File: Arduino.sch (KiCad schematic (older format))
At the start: 23 parts

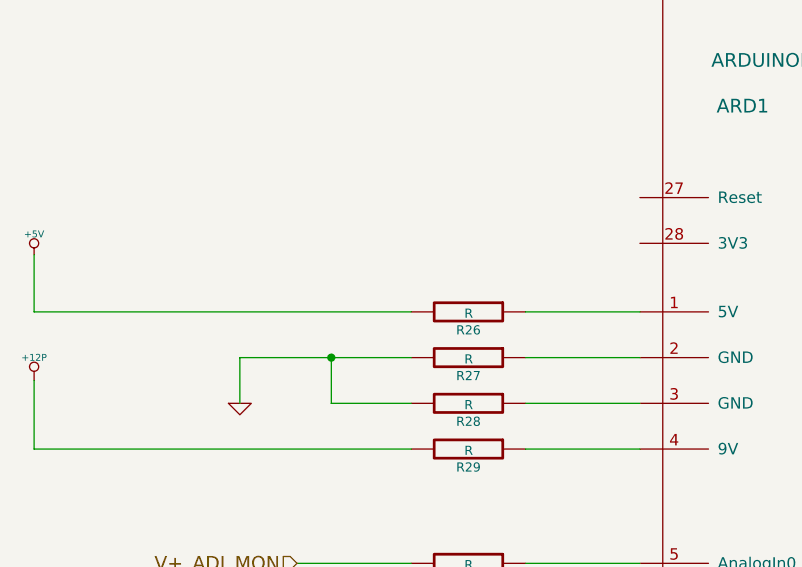
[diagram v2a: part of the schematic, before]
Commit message: Layout Work Session 16
Added ground connect to heatsink, fixed relay trace width, fixed silk
screen issues.
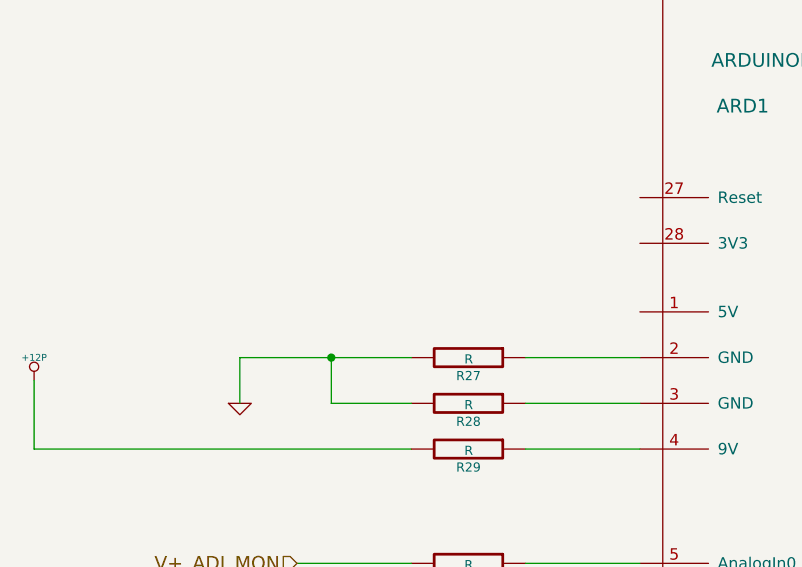
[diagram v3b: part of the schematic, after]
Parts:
- removed R26: R, ~, symbol R
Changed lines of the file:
@@
-EESchema Schematic File Version 2  date 11/24/2013 8:21:44 PM
+EESchema Schematic File Version 2  date 12/1/2013 9:10:28 PM
 LIBS:power
 LIBS:device
@@
 Sheet 8 9
 Title ""
-Date "24 nov 2013"
+Date "2 dec 2013"
 Rev ""
 Comp ""
@@
 	8500 5700 8500 6100
 $Comp
-L GND #PWR041
+L GND #PWR52
 U 1 1 524020EC
 P 8500 6100
-F 0 "#PWR041" H 8500 6100 30  0001 C CNN
+F 0 "#PWR52" H 8500 6100 30  0001 C CNN
 F 1 "GND" H 8500 6030 30  0001 C CNN
 F 2 "~" H 8500 6100 60  0000 C CNN
@@
 	3350 4350 3850 4350
 $Comp
-L +12P #PWR042
+L +12P #PWR50
 U 1 1 5243CFCD
 P 1200 4050
-F 0 "#PWR042" H 1200 4020 30  0001 C CNN
+F 0 "#PWR50" H 1200 4020 30  0001 C CNN
 F 1 "+12P" H 1200 4150 30  0000 C CNN
 F 2 "~" H 1200 4050 60  0000 C CNN
@@
 Wire Wire Line
 	1200 4350 2850 4350
-$Comp
-L R R26
-U 1 1 5245171E
-P 3100 3750
-F 0 "R26" V 3180 3750 40  0000 C CNN
-F 1 "R" V 3107 3751 40  0000 C CNN
-F 2 "~" V 3030 3750 30  0000 C CNN
-F 3 "~" H 3100 3750 30  0000 C CNN
-	1    3100 3750
-	0    1    1    0
-$EndComp
-Wire Wire Line
-	3350 3750 3850 3750
-$Comp
-L +5V #PWR043
-U 1 1 5245176C
-P 1200 3500
-F 0 "#PWR043" H 1200 3590 20  0001 C CNN
-F 1 "+5V" H 1200 3590 30  0000 C CNN
-F 2 "~" H 1200 3500 60  0000 C CNN
-F 3 "~" H 1200 3500 60  0000 C CNN
-	1    1200 3500
-	1    0    0    -1
-$EndComp
-Wire Wire Line
-	2850 3750 1200 3750
-Wire Wire Line
-	1200 3750 1200 3500
 Wire Wire Line
 	3850 3950 3350 3950
@@
 	2100 3950 2100 4150
 $Comp
-L GND #PWR044
+L GND #PWR51
 U 1 1 5245181B
 P 2100 4150
-F 0 "#PWR044" H 2100 4150 30  0001 C CNN
+F 0 "#PWR51" H 2100 4150 30  0001 C CNN
 F 1 "GND" H 2100 4080 30  0001 C CNN
 F 2 "~" H 2100 4150 60  0000 C CNN

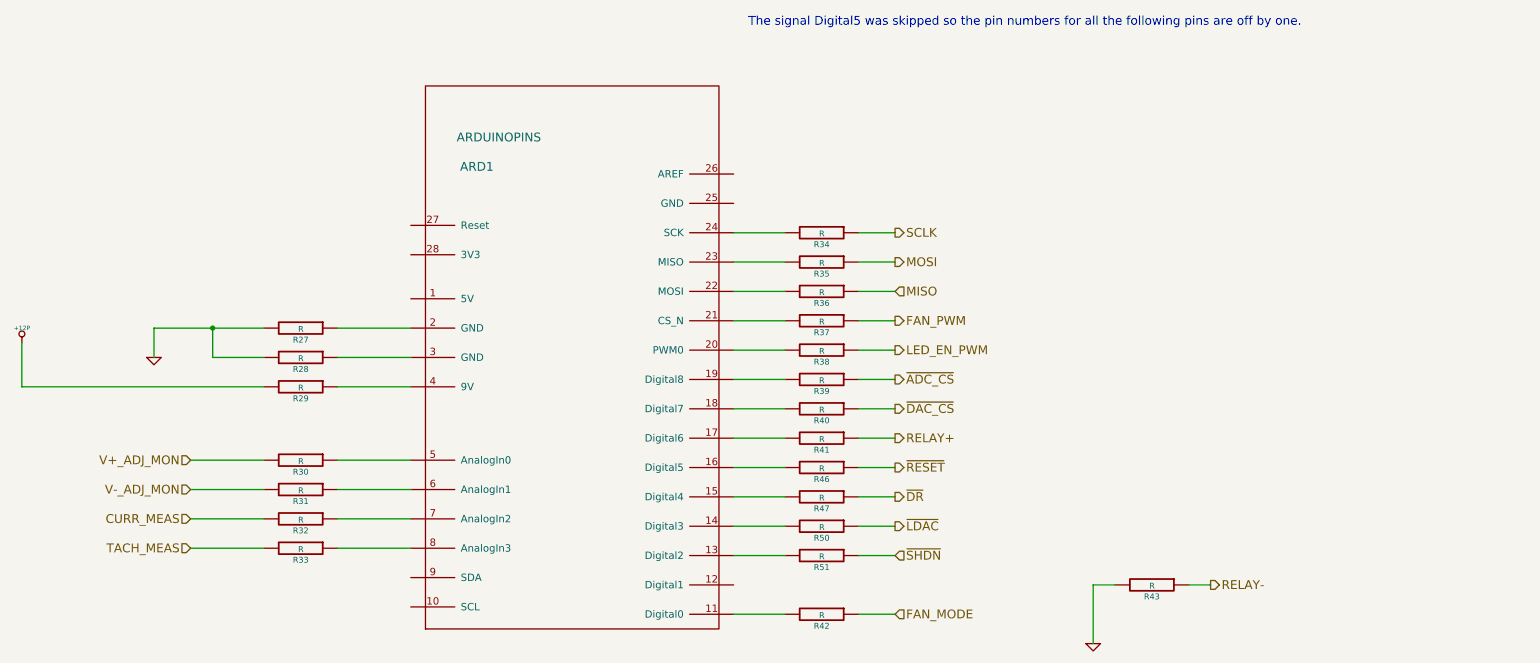
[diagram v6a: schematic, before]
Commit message: Added Passive Values and SPICE models
As part of week 1 of Session 1B, we added a SPICE model of the In amp
and went through and assigned values to all of the passive components.
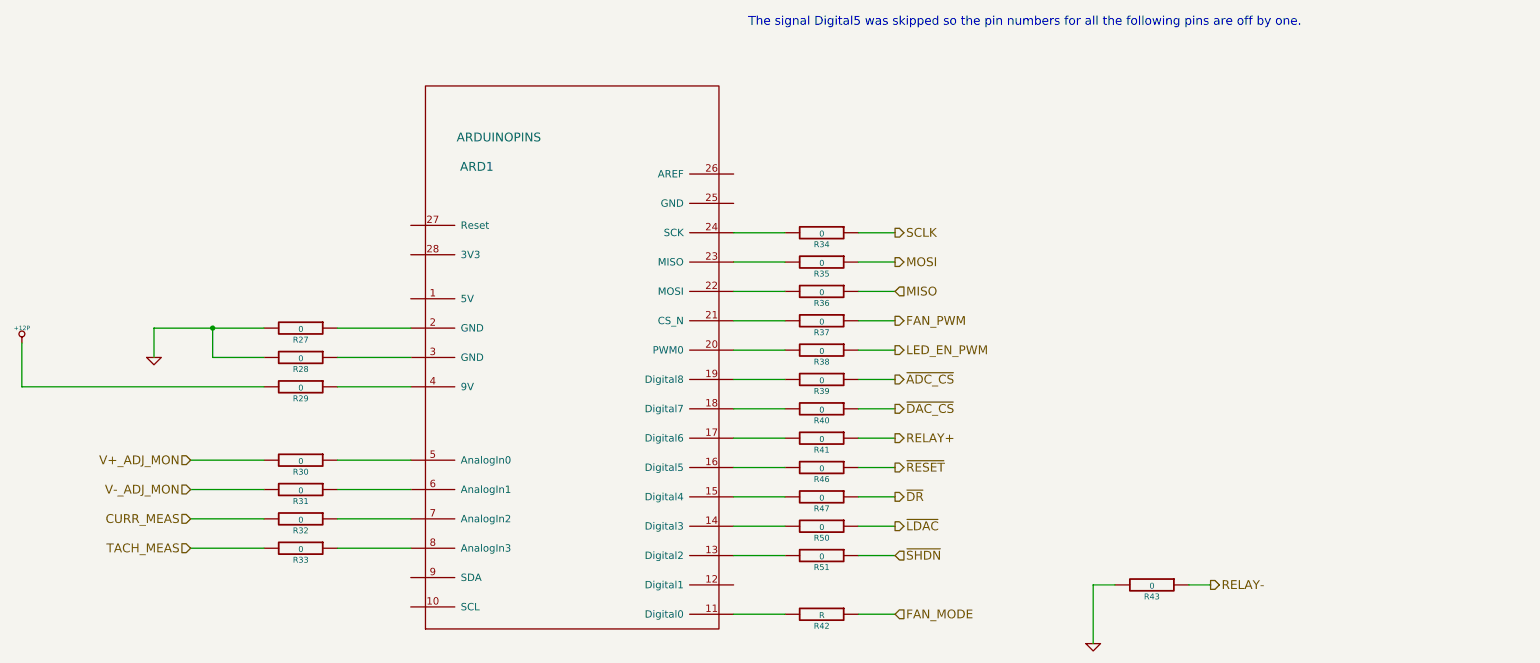
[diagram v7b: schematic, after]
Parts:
- R27, R28, R29, R30, R31, R32, R33, R34, R35, R36, R37, R38, R39, R40, R41, R43, R46, R47, R50, R51: value R -> 0
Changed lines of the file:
@@
-EESchema Schematic File Version 2  date 2/16/2014 3:41:32 PM
+EESchema Schematic File Version 2  date 4/16/2014 11:04:06 PM
 LIBS:power
 LIBS:device
@@
 Sheet 8 9
 Title ""
-Date "16 feb 2014"
+Date "17 apr 2014"
 Rev ""
 Comp ""
@@
 P 6650 3900
 F 0 "R37" V 6730 3900 40  0000 C CNN
-F 1 "R" V 6657 3901 40  0000 C CNN
+F 1 "0" V 6657 3901 40  0000 C CNN
 F 2 "~" V 6580 3900 30  0000 C CNN
 F 3 "~" H 6650 3900 30  0000 C CNN
@@
 P 6650 4700
 F 0 "R41" V 6730 4700 40  0000 C CNN
-F 1 "R" V 6657 4701 40  0000 C CNN
+F 1 "0" V 6657 4701 40  0000 C CNN
 F 2 "~" V 6580 4700 30  0000 C CNN
 F 3 "~" H 6650 4700 30  0000 C CNN
@@
 P 3100 5250
 F 0 "R32" V 3180 5250 40  0000 C CNN
-F 1 "R" V 3107 5251 40  0000 C CNN
+F 1 "0" V 3107 5251 40  0000 C CNN
 F 2 "~" V 3030 5250 30  0000 C CNN
 F 3 "~" H 3100 5250 30  0000 C CNN
@@
 P 3100 5450
 F 0 "R33" V 3180 5450 40  0000 C CNN
-F 1 "R" V 3107 5451 40  0000 C CNN
+F 1 "0" V 3107 5451 40  0000 C CNN
 F 2 "~" V 3030 5450 30  0000 C CNN
 F 3 "~" H 3100 5450 30  0000 C CNN
@@
 P 3100 5050
 F 0 "R31" V 3180 5050 40  0000 C CNN
-F 1 "R" V 3107 5051 40  0000 C CNN
+F 1 "0" V 3107 5051 40  0000 C CNN
 F 2 "~" V 3030 5050 30  0000 C CNN
 F 3 "~" H 3100 5050 30  0000 C CNN
@@
 P 3100 4850
 F 0 "R30" V 3180 4850 40  0000 C CNN
-F 1 "R" V 3107 4851 40  0000 C CNN
+F 1 "0" V 3107 4851 40  0000 C CNN
 F 2 "~" V 3030 4850 30  0000 C CNN
 F 3 "~" H 3100 4850 30  0000 C CNN
@@
 P 6650 3300
 F 0 "R34" V 6730 3300 40  0000 C CNN
-F 1 "R" V 6657 3301 40  0000 C CNN
+F 1 "0" V 6657 3301 40  0000 C CNN
 F 2 "~" V 6580 3300 30  0000 C CNN
 F 3 "~" H 6650 3300 30  0000 C CNN
@@
 P 6650 3500
 F 0 "R35" V 6730 3500 40  0000 C CNN
-F 1 "R" V 6657 3501 40  0000 C CNN
+F 1 "0" V 6657 3501 40  0000 C CNN
 F 2 "~" V 6580 3500 30  0000 C CNN
 F 3 "~" H 6650 3500 30  0000 C CNN
@@
 P 6650 3700
 F 0 "R36" V 6730 3700 40  0000 C CNN
-F 1 "R" V 6657 3701 40  0000 C CNN
+F 1 "0" V 6657 3701 40  0000 C CNN
 F 2 "~" V 6580 3700 30  0000 C CNN
 F 3 "~" H 6650 3700 30  0000 C CNN
@@
 P 6650 4500
 F 0 "R40" V 6730 4500 40  0000 C CNN
-F 1 "R" V 6657 4501 40  0000 C CNN
+F 1 "0" V 6657 4501 40  0000 C CNN
 F 2 "~" V 6580 4500 30  0000 C CNN
 F 3 "~" H 6650 4500 30  0000 C CNN
@@
 P 8900 5700
 F 0 "R43" V 8980 5700 40  0000 C CNN
-F 1 "R" V 8907 5701 40  0000 C CNN
+F 1 "0" V 8907 5701 40  0000 C CNN
 F 2 "~" V 8830 5700 30  0000 C CNN
 F 3 "~" H 8900 5700 30  0000 C CNN
@@
 P 6650 4100
 F 0 "R38" V 6730 4100 40  0000 C CNN
-F 1 "R" V 6657 4101 40  0000 C CNN
+F 1 "0" V 6657 4101 40  0000 C CNN
 F 2 "~" V 6580 4100 30  0000 C CNN
 F 3 "~" H 6650 4100 30  0000 C CNN
@@
 P 6650 4300
 F 0 "R39" V 6730 4300 40  0000 C CNN
-F 1 "R" V 6657 4301 40  0000 C CNN
+F 1 "0" V 6657 4301 40  0000 C CNN
 F 2 "~" V 6580 4300 30  0000 C CNN
 F 3 "~" H 6650 4300 30  0000 C CNN
@@
 P 3100 4350
 F 0 "R29" V 3180 4350 40  0000 C CNN
-F 1 "R" V 3107 4351 40  0000 C CNN
+F 1 "0" V 3107 4351 40  0000 C CNN
 F 2 "~" V 3030 4350 30  0000 C CNN
 F 3 "~" H 3100 4350 30  0000 C CNN
@@
 P 3100 3950
 F 0 "R27" V 3180 3950 40  0000 C CNN
-F 1 "R" V 3107 3951 40  0000 C CNN
+F 1 "0" V 3107 3951 40  0000 C CNN
 F 2 "~" V 3030 3950 30  0000 C CNN
 F 3 "~" H 3100 3950 30  0000 C CNN
@@
 P 3100 4150
 F 0 "R28" V 3180 4150 40  0000 C CNN
-F 1 "R" V 3107 4151 40  0000 C CNN
+F 1 "0" V 3107 4151 40  0000 C CNN
 F 2 "~" V 3030 4150 30  0000 C CNN
 F 3 "~" H 3100 4150 30  0000 C CNN
@@
 P 6650 4900
 F 0 "R46" V 6730 4900 40  0000 C CNN
-F 1 "R" V 6657 4901 40  0000 C CNN
+F 1 "0" V 6657 4901 40  0000 C CNN
 F 2 "~" V 6580 4900 30  0000 C CNN
 F 3 "~" H 6650 4900 30  0000 C CNN
@@
 P 6650 5100
 F 0 "R47" V 6730 5100 40  0000 C CNN
-F 1 "R" V 6657 5101 40  0000 C CNN
+F 1 "0" V 6657 5101 40  0000 C CNN
 F 2 "~" V 6580 5100 30  0000 C CNN
 F 3 "~" H 6650 5100 30  0000 C CNN
@@
 P 6650 5300
 F 0 "R50" V 6730 5300 40  0000 C CNN
-F 1 "R" V 6657 5301 40  0000 C CNN
+F 1 "0" V 6657 5301 40  0000 C CNN
 F 2 "~" V 6580 5300 30  0000 C CNN
 F 3 "~" H 6650 5300 30  0000 C CNN
@@
 P 6650 5500
 F 0 "R51" V 6730 5500 40  0000 C CNN
-F 1 "R" V 6657 5501 40  0000 C CNN
+F 1 "0" V 6657 5501 40  0000 C CNN
 F 2 "~" V 6580 5500 30  0000 C CNN
 F 3 "~" H 6650 5500 30  0000 C CNN

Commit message: Added the schematic and BOM changes back in after hard reset
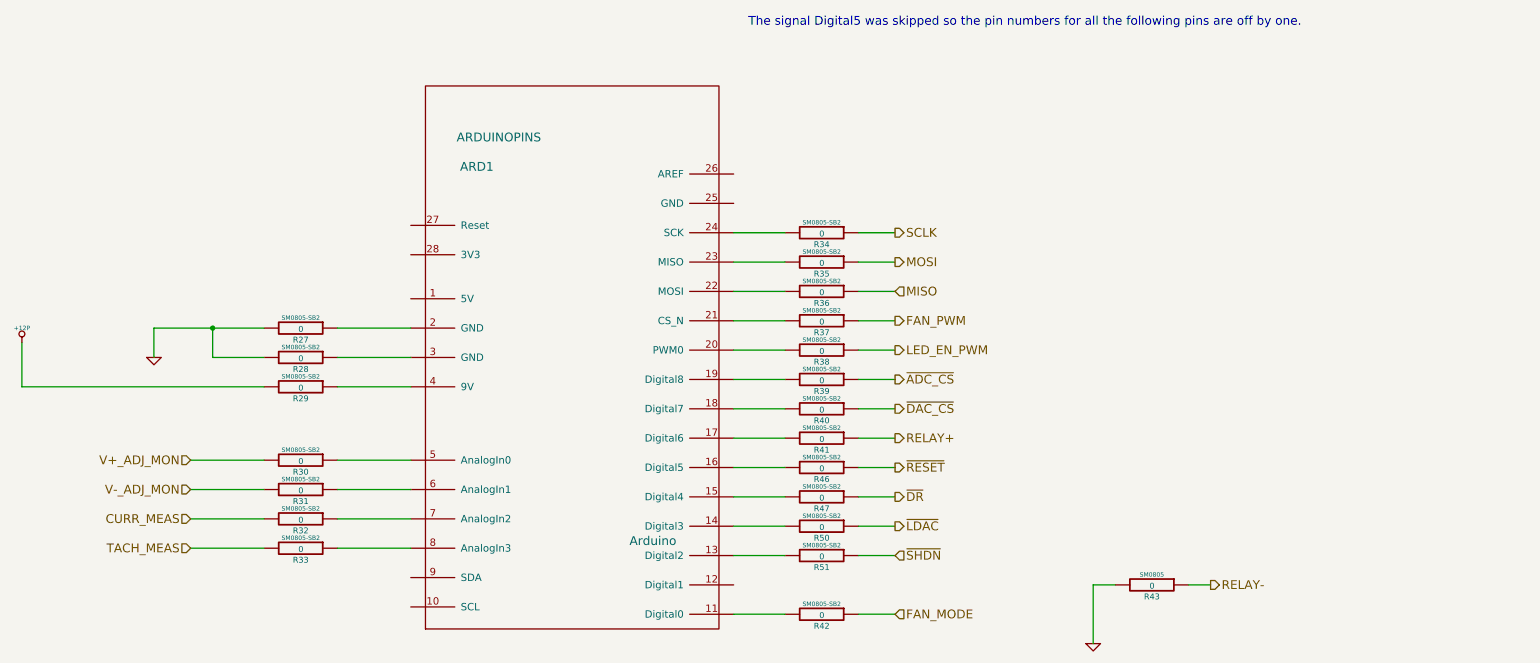
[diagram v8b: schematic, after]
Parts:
- ARD1: footprint ~ -> Arduino
- R27, R28, R29, R30, R31, R32, R33, R34, R35, R36, R37, R38, R39, R40, R41, R46, R47, R50, R51: footprint ~ -> SM0805-SB2
- R42: value R -> 0; footprint ~ -> SM0805-SB2
- R43: footprint ~ -> SM0805
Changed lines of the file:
@@
-EESchema Schematic File Version 2  date 4/16/2014 11:04:06 PM
+EESchema Schematic File Version 2  date 4/18/2014 9:49:53 PM
 LIBS:power
 LIBS:device
@@
 Sheet 8 9
 Title ""
-Date "17 apr 2014"
+Date "19 apr 2014"
 Rev ""
 Comp ""
@@
 F 0 "R37" V 6730 3900 40  0000 C CNN
 F 1 "0" V 6657 3901 40  0000 C CNN
-F 2 "~" V 6580 3900 30  0000 C CNN
+F 2 "SM0805-SB2" V 6580 3900 30  0000 C CNN
 F 3 "~" H 6650 3900 30  0000 C CNN
 	1    6650 3900
@@
 F 0 "R41" V 6730 4700 40  0000 C CNN
 F 1 "0" V 6657 4701 40  0000 C CNN
-F 2 "~" V 6580 4700 30  0000 C CNN
+F 2 "SM0805-SB2" V 6580 4700 30  0000 C CNN
 F 3 "~" H 6650 4700 30  0000 C CNN
 	1    6650 4700
@@
 F 0 "R32" V 3180 5250 40  0000 C CNN
 F 1 "0" V 3107 5251 40  0000 C CNN
-F 2 "~" V 3030 5250 30  0000 C CNN
+F 2 "SM0805-SB2" V 3030 5250 30  0000 C CNN
 F 3 "~" H 3100 5250 30  0000 C CNN
 	1    3100 5250
@@
 F 0 "R33" V 3180 5450 40  0000 C CNN
 F 1 "0" V 3107 5451 40  0000 C CNN
-F 2 "~" V 3030 5450 30  0000 C CNN
+F 2 "SM0805-SB2" V 3030 5450 30  0000 C CNN
 F 3 "~" H 3100 5450 30  0000 C CNN
 	1    3100 5450
@@
 F 0 "R31" V 3180 5050 40  0000 C CNN
 F 1 "0" V 3107 5051 40  0000 C CNN
-F 2 "~" V 3030 5050 30  0000 C CNN
+F 2 "SM0805-SB2" V 3030 5050 30  0000 C CNN
 F 3 "~" H 3100 5050 30  0000 C CNN
 	1    3100 5050
@@
 F 0 "R30" V 3180 4850 40  0000 C CNN
 F 1 "0" V 3107 4851 40  0000 C CNN
-F 2 "~" V 3030 4850 30  0000 C CNN
+F 2 "SM0805-SB2" V 3030 4850 30  0000 C CNN
 F 3 "~" H 3100 4850 30  0000 C CNN
 	1    3100 4850
@@
 F 0 "R34" V 6730 3300 40  0000 C CNN
 F 1 "0" V 6657 3301 40  0000 C CNN
-F 2 "~" V 6580 3300 30  0000 C CNN
+F 2 "SM0805-SB2" V 6580 3300 30  0000 C CNN
 F 3 "~" H 6650 3300 30  0000 C CNN
 	1    6650 3300
@@
 F 0 "R35" V 6730 3500 40  0000 C CNN
 F 1 "0" V 6657 3501 40  0000 C CNN
-F 2 "~" V 6580 3500 30  0000 C CNN
+F 2 "SM0805-SB2" V 6580 3500 30  0000 C CNN
 F 3 "~" H 6650 3500 30  0000 C CNN
 	1    6650 3500
@@
 F 0 "R36" V 6730 3700 40  0000 C CNN
 F 1 "0" V 6657 3701 40  0000 C CNN
-F 2 "~" V 6580 3700 30  0000 C CNN
+F 2 "SM0805-SB2" V 6580 3700 30  0000 C CNN
 F 3 "~" H 6650 3700 30  0000 C CNN
 	1    6650 3700
@@
 F 0 "R40" V 6730 4500 40  0000 C CNN
 F 1 "0" V 6657 4501 40  0000 C CNN
-F 2 "~" V 6580 4500 30  0000 C CNN
+F 2 "SM0805-SB2" V 6580 4500 30  0000 C CNN
 F 3 "~" H 6650 4500 30  0000 C CNN
 	1    6650 4500
@@
 F 0 "R43" V 8980 5700 40  0000 C CNN
 F 1 "0" V 8907 5701 40  0000 C CNN
-F 2 "~" V 8830 5700 30  0000 C CNN
+F 2 "SM0805" V 8830 5700 30  0000 C CNN
 F 3 "~" H 8900 5700 30  0000 C CNN
 	1    8900 5700
@@
 F 0 "R38" V 6730 4100 40  0000 C CNN
 F 1 "0" V 6657 4101 40  0000 C CNN
-F 2 "~" V 6580 4100 30  0000 C CNN
+F 2 "SM0805-SB2" V 6580 4100 30  0000 C CNN
 F 3 "~" H 6650 4100 30  0000 C CNN
 	1    6650 4100
@@
 F 0 "R39" V 6730 4300 40  0000 C CNN
 F 1 "0" V 6657 4301 40  0000 C CNN
-F 2 "~" V 6580 4300 30  0000 C CNN
+F 2 "SM0805-SB2" V 6580 4300 30  0000 C CNN
 F 3 "~" H 6650 4300 30  0000 C CNN
 	1    6650 4300
@@
 P 6650 5900
 F 0 "R42" V 6730 5900 40  0000 C CNN
-F 1 "R" V 6657 5901 40  0000 C CNN
-F 2 "~" V 6580 5900 30  0000 C CNN
+F 1 "0" V 6657 5901 40  0000 C CNN
+F 2 "SM0805-SB2" V 6580 5900 30  0000 C CNN
 F 3 "~" H 6650 5900 30  0000 C CNN
 	1    6650 5900
@@
 F 0 "R29" V 3180 4350 40  0000 C CNN
 F 1 "0" V 3107 4351 40  0000 C CNN
-F 2 "~" V 3030 4350 30  0000 C CNN
+F 2 "SM0805-SB2" V 3030 4350 30  0000 C CNN
 F 3 "~" H 3100 4350 30  0000 C CNN
 	1    3100 4350
@@
 F 0 "R27" V 3180 3950 40  0000 C CNN
 F 1 "0" V 3107 3951 40  0000 C CNN
-F 2 "~" V 3030 3950 30  0000 C CNN
+F 2 "SM0805-SB2" V 3030 3950 30  0000 C CNN
 F 3 "~" H 3100 3950 30  0000 C CNN
 	1    3100 3950
@@
 F 0 "R28" V 3180 4150 40  0000 C CNN
 F 1 "0" V 3107 4151 40  0000 C CNN
-F 2 "~" V 3030 4150 30  0000 C CNN
+F 2 "SM0805-SB2" V 3030 4150 30  0000 C CNN
 F 3 "~" H 3100 4150 30  0000 C CNN
 	1    3100 4150
@@
 F 0 "ARD1" H 4300 6050 60  0000 C CNN
 F 1 "ARDUINOPINS" H 4450 6250 60  0000 C CNN
-F 2 "~" H 5500 3500 60  0000 C CNN
+F 2 "Arduino" H 5500 3500 60  0000 C CNN
 F 3 "~" H 5500 3500 60  0000 C CNN
 	1    4950 4450
@@
 F 0 "R46" V 6730 4900 40  0000 C CNN
 F 1 "0" V 6657 4901 40  0000 C CNN
-F 2 "~" V 6580 4900 30  0000 C CNN
+F 2 "SM0805-SB2" V 6580 4900 30  0000 C CNN
 F 3 "~" H 6650 4900 30  0000 C CNN
 	1    6650 4900
@@
 F 0 "R47" V 6730 5100 40  0000 C CNN
 F 1 "0" V 6657 5101 40  0000 C CNN
-F 2 "~" V 6580 5100 30  0000 C CNN
+F 2 "SM0805-SB2" V 6580 5100 30  0000 C CNN
 F 3 "~" H 6650 5100 30  0000 C CNN
 	1    6650 5100
@@
 F 0 "R50" V 6730 5300 40  0000 C CNN
 F 1 "0" V 6657 5301 40  0000 C CNN
-F 2 "~" V 6580 5300 30  0000 C CNN
+F 2 "SM0805-SB2" V 6580 5300 30  0000 C CNN
 F 3 "~" H 6650 5300 30  0000 C CNN
 	1    6650 5300
@@
 F 0 "R51" V 6730 5500 40  0000 C CNN
 F 1 "0" V 6657 5501 40  0000 C CNN
-F 2 "~" V 6580 5500 30  0000 C CNN
+F 2 "SM0805-SB2" V 6580 5500 30  0000 C CNN
 F 3 "~" H 6650 5500 30  0000 C CNN
 	1    6650 5500
